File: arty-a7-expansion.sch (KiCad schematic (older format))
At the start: 61 parts, among them IC1 TPD8S009DSMR, J2 1140084168, J4 685119134923, J5 UE27AC54100, U1 TPS61232DRCT, U2 MAX3421EEHJ, Y1 KX-7_12.MHz

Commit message: Introduced schematic sections
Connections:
- net +3V3: now also C19.2; no longer C19.1
- net GND: now also C19.1; no longer C19.2
- net XI: now reaches C16.1, U2.24 (XI), Y1.1
- net XO: now reaches C17.1, U2.25 (XO), Y1.3
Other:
- note added: "Arty PMOD Connectors"
- note added: "USB controller"
- note removed: "HDMI Pmod connector"
- note removed: "SD card Pmod connector"
- note removed: "USB Pmod connector"
- moved on the sheet: C1, C10, C11, C12, C13, C14, C15, C16, C17, C18, C19, D1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

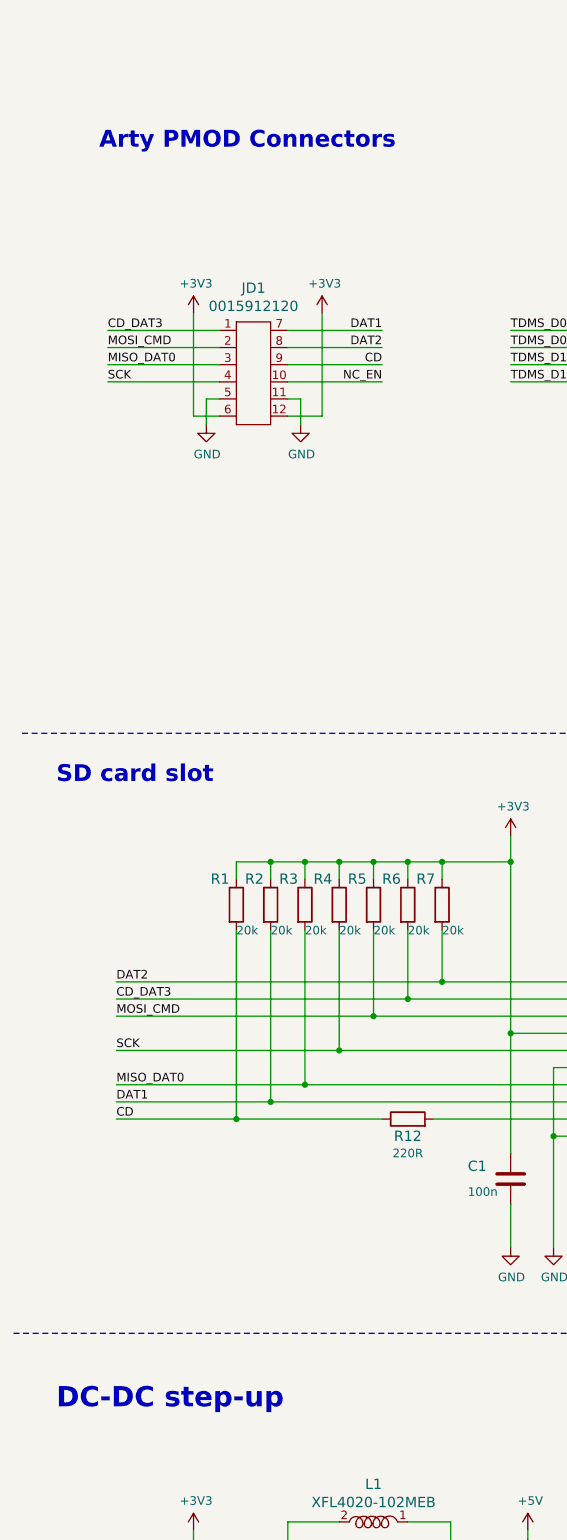
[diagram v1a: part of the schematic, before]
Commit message: Updated U1 MPN, updated layout around IC1
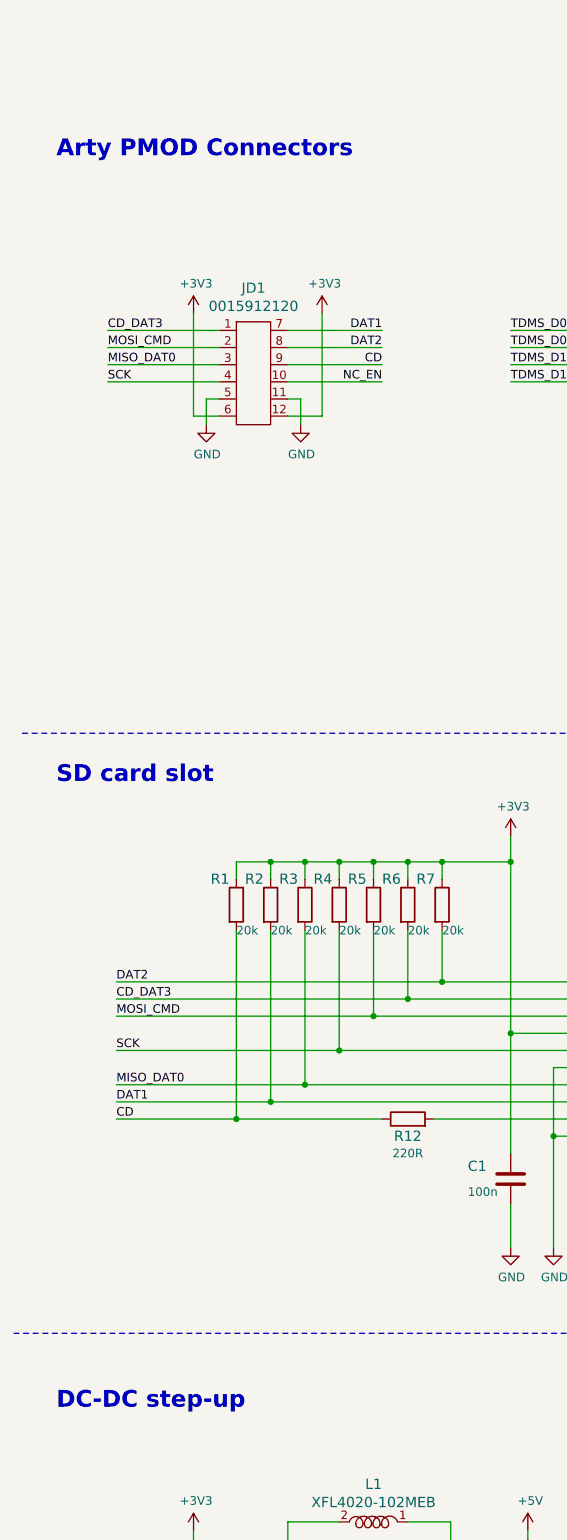
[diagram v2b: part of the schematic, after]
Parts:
- U1: MPN (none) -> TPS61232DRCT; Manufacturer (none) -> Texas Instruments

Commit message: Minor changes
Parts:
- added R23: R_0R_0603, arty-a7-expansion-footprints:0603-res, symbol arty-a7-expansion:R_0R_0603
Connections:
- net +3V3: now also R23.1
- net RST_USB: now also R23.2
- net D+: no longer names the net of R10.2, U2.21 (D+)
- net D-: no longer names the net of R9.2, U2.20 (D-)
- no-connect marks 0 -> 1
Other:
- note added: "DNP"
- moved on the sheet: J5, R10, R11, R9
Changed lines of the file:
@@
 $EndComp
-Wire Wire Line
-	12100 6950 11250 6950
 Wire Wire Line
 	12100 7050 11250 7050
@@
 Wire Wire Line
 	12100 7450 11250 7450
-Text Label 11250 6950 0    50   ~ 0
-RST_USB
 Text Label 11250 7050 0    50   ~ 0
 SCK_USB
@@
 	12700 5750 12700 5600
 Wire Wire Line
-	12100 6150 11850 6150
+	12100 6150 11950 6150
 $Comp
 L arty-a7-expansion:R_22R_0402 R9
 U 1 1 5D7A374A
-P 11350 6350
-F 0 "R9" H 11050 6400 60  0000 C CNN
-F 1 "R_22R_0402" H 11350 6200 60  0001 C CNN
-F 2 "arty-a7-expansion-footprints:0402-res" H 11550 6550 60  0001 L CNN
-F 3 "" H 11350 6350 50  0001 C CNN
-F 4 "VISHAY" H 11550 6750 60  0001 L CNN "Manufacturer"
-F 5 "CRCW040222R0FKED" H 11550 6650 60  0001 L CNN "MPN"
-F 6 "22R" H 11325 6350 50  0000 C CNN "Val"
-	1    11350 6350
+P 10650 6350
+F 0 "R9" H 10350 6400 60  0000 C CNN
+F 1 "R_22R_0402" H 10650 6200 60  0001 C CNN
+F 2 "arty-a7-expansion-footprints:0402-res" H 10850 6550 60  0001 L CNN
+F 3 "" H 10650 6350 50  0001 C CNN
+F 4 "VISHAY" H 10850 6750 60  0001 L CNN "Manufacturer"
+F 5 "CRCW040222R0FKED" H 10850 6650 60  0001 L CNN "MPN"
+F 6 "22R" H 10625 6350 50  0000 C CNN "Val"
+	1    10650 6350
 	1    0    0    -1
 $EndComp
@@
 L arty-a7-expansion:R_22R_0402 R10
 U 1 1 5D7A394F
-P 11350 6450
-F 0 "R10" H 11075 6375 60  0000 C CNN
-F 1 "R_22R_0402" H 11350 6300 60  0001 C CNN
-F 2 "arty-a7-expansion-footprints:0402-res" H 11550 6650 60  0001 L CNN
-F 3 "" H 11350 6450 50  0001 C CNN
-F 4 "VISHAY" H 11550 6850 60  0001 L CNN "Manufacturer"
-F 5 "CRCW040222R0FKED" H 11550 6750 60  0001 L CNN "MPN"
-F 6 "22R" H 11350 6450 50  0000 C CNN "Val"
-	1    11350 6450
+P 10650 6450
+F 0 "R10" H 10375 6375 60  0000 C CNN
+F 1 "R_22R_0402" H 10650 6300 60  0001 C CNN
+F 2 "arty-a7-expansion-footprints:0402-res" H 10850 6650 60  0001 L CNN
+F 3 "" H 10650 6450 50  0001 C CNN
+F 4 "VISHAY" H 10850 6850 60  0001 L CNN "Manufacturer"
+F 5 "CRCW040222R0FKED" H 10850 6750 60  0001 L CNN "MPN"
+F 6 "22R" H 10650 6450 50  0000 C CNN "Val"
+	1    10650 6450
 	1    0    0    -1
 $EndComp
@@
 L arty-a7-expansion:UE27AC54100 J5
 U 1 1 5D7BA5ED
-P 9050 6350
-F 0 "J5" V 8800 6650 60  0000 C CNN
-F 1 "UE27AC54100" V 8900 6400 60  0000 C CNN
-F 2 "arty-a7-expansion-footprints:USB_A_Female_UE27AC54100" H 9250 6550 60  0001 L CNN
-F 3 "https://www.amphenolcanada.com/ProductSearch/drawings/AC/UE27ACX4X0X.pdf" H 9250 6650 60  0001 L CNN
-F 4 "UE27AC54100" H 9250 6850 60  0001 L CNN "MPN"
-F 5 "Amphenol ICC (Commercial Products)" H 9250 7450 60  0001 L CNN "Manufacturer"
-	1    9050 6350
+P 8900 6350
+F 0 "J5" V 8650 6650 60  0000 C CNN
+F 1 "UE27AC54100" V 8750 6400 60  0000 C CNN
+F 2 "arty-a7-expansion-footprints:USB_A_Female_UE27AC54100" H 9100 6550 60  0001 L CNN
+F 3 "https://www.amphenolcanada.com/ProductSearch/drawings/AC/UE27ACX4X0X.pdf" H 9100 6650 60  0001 L CNN
+F 4 "UE27AC54100" H 9100 6850 60  0001 L CNN "MPN"
+F 5 "Amphenol ICC (Commercial Products)" H 9100 7450 60  0001 L CNN "Manufacturer"
+	1    8900 6350
 	1    0    0    1
 $EndComp
 Wire Wire Line
-	9500 6550 9350 6550
+	9500 6550 9200 6550
 $Comp
 L arty-a7-expansion:GND #PWR0109
@@
 $EndComp
 Wire Wire Line
-	9350 6450 9700 6450
+	9200 6450 9700 6450
 Wire Wire Line
 	9700 6450 9700 6600
@@
 	1500 10500 1500 10400
 Wire Wire Line
-	11850 6150 11850 6100
-Wire Wire Line
 	2200 10150 2100 10150
 Wire Wire Line
@@
 $EndComp
 Wire Wire Line
-	9350 6250 9350 5850
+	9200 6250 9200 5850
 $Comp
 L arty-a7-expansion:+5V #PWR0117
@@
 L arty-a7-expansion:R_10k_0603 R11
 U 1 1 5D77F979
-P 11850 5950
-F 0 "R11" V 11805 6020 60  0000 L CNN
-F 1 "R_10k_0603" H 11850 5800 60  0001 C CNN
-F 2 "arty-a7-expansion-footprints:0603-res" H 12050 6150 60  0001 L CNN
-F 3 "" H 11850 5950 50  0001 C CNN
-F 4 "BOURNS" H 12050 6350 60  0001 L CNN "Manufacturer"
-F 5 "CR0603-JW-103ELF" H 12050 6250 60  0001 L CNN "MPN"
-F 6 "10k" V 11903 6020 50  0000 L CNN "Val"
-	1    11850 5950
+P 11950 5500
+F 0 "R11" V 11800 5500 60  0000 L CNN
+F 1 "R_10k_0603" H 11950 5350 60  0001 C CNN
+F 2 "arty-a7-expansion-footprints:0603-res" H 12150 5700 60  0001 L CNN
+F 3 "" H 11950 5500 50  0001 C CNN
+F 4 "BOURNS" H 12150 5900 60  0001 L CNN "Manufacturer"
+F 5 "CR0603-JW-103ELF" H 12150 5800 60  0001 L CNN "MPN"
+F 6 "10k" V 12003 5570 50  0000 L CNN "Val"
+	1    11950 5500
 	0    1    1    0
 $EndComp
 Text Label 6950 2350 0    50   ~ 0
 GPX_USB
-Wire Wire Line
-	11850 6150 11250 6150
-Connection ~ 11850 6150
+Connection ~ 11950 6150
 Text Label 11250 6150 0    50   ~ 0
 INT_USB
 Text Label 7300 2550 2    50   ~ 0
 INT_USB
-$Comp
-L arty-a7-expansion:TP_SMD1MM TP5
-U 1 1 5D79AD74
-P 11150 6950
-F 0 "TP5" V 11150 6850 50  0000 C CNN
-F 1 "TP_SMD1MM" H 11150 6850 50  0001 C CNN
-F 2 "arty-a7-expansion-footprints:Testpoint_smd_1mm" H 11350 7150 60  0001 L CNN
-F 3 "" H 11350 7250 60  0001 L CNN
-	1    11150 6950
-	0    1    1    0
-$EndComp
 $Comp
 L arty-a7-expansion:TP_SMD1MM TP6
@@
 	1    0    0    -1
 $EndComp
-Text Label 11625 6450 0    50   ~ 0
-D+
-Text Label 11625 6350 0    50   ~ 0
-D-
-Text Label 10350 6350 0    50   ~ 0
+Text Label 9250 6350 0    50   ~ 0
 Data-
-Text Label 10350 6450 0    50   ~ 0
+Text Label 9250 6450 0    50   ~ 0
 Data+
 $Comp
@@
 	2900 6950 3900 6950
 Wire Wire Line
-	9175 6025 9500 6025
+	9025 6025 9500 6025
 Wire Wire Line
 	9500 6025 9500 6550
@@
 	9500 6550 9500 7150
 Wire Wire Line
-	11500 6450 12100 6450
-Wire Wire Line
-	11500 6350 12100 6350
+	10800 6450 12100 6450
+Wire Wire Line
+	10800 6350 12100 6350
 $Comp
 L arty-a7-expansion:+3V3 #PWR0112
@@
 	7750 8950 16050 8950
 Wire Wire Line
-	9700 6450 11200 6450
-Wire Wire Line
-	9350 6350 10000 6350
+	9700 6450 10500 6450
+Wire Wire Line
+	9200 6350 10000 6350
 Wire Wire Line
 	10000 6600 10000 6350
 Connection ~ 10000 6350
 Wire Wire Line
-	10000 6350 11200 6350
+	10000 6350 10500 6350
 $Comp
 L arty-a7-expansion:GND #PWR0131
@@
 	13750 5600 13750 5650
 $Comp
-L arty-a7-expansion:+3V3 #PWR0134
-U 1 1 5E79E54F
-P 11850 5600
-F 0 "#PWR0134" H 11850 5450 50  0001 C CNN
-F 1 "+3V3" H 11865 5773 50  0000 C CNN
-F 2 "" H 11850 5600 50  0001 C CNN
-F 3 "" H 11850 5600 50  0001 C CNN
-	1    11850 5600
-	1    0    0    -1
-$EndComp
-Wire Wire Line
-	11850 5600 11850 5800
-$Comp
 L arty-a7-expansion:GND #PWR0135
 U 1 1 5E7B2037
@@
 L arty-a7-expansion:+5V #PWR0138
 U 1 1 5E7FF960
-P 9350 5850
-F 0 "#PWR0138" H 9350 5700 50  0001 C CNN
-F 1 "+5V" H 9365 6023 50  0000 C CNN
-F 2 "" H 9350 5850 50  0001 C CNN
-F 3 "" H 9350 5850 50  0001 C CNN
-	1    9350 5850
+P 9200 5850
+F 0 "#PWR0138" H 9200 5700 50  0001 C CNN
+F 1 "+5V" H 9215 6023 50  0000 C CNN
+F 2 "" H 9200 5850 50  0001 C CNN
+F 3 "" H 9200 5850 50  0001 C CNN
+	1    9200 5850
 	1    0    0    -1
 $EndComp
@@
 	1    0    0    -1
 $EndComp
+NoConn ~ 9950 3000
+Text Label 11250 6950 0    50   ~ 0
+RST_USB
+$Comp
+L arty-a7-expansion:TP_SMD1MM TP5
+U 1 1 5D79AD74
+P 11150 6950
+F 0 "TP5" V 11150 6850 50  0000 C CNN
+F 1 "TP_SMD1MM" H 11150 6850 50  0001 C CNN
+F 2 "arty-a7-expansion-footprints:Testpoint_smd_1mm" H 11350 7150 60  0001 L CNN
+F 3 "" H 11350 7250 60  0001 L CNN
+	1    11150 6950
+	0    1    1    0
+$EndComp
+$Comp
+L arty-a7-expansion:R_0R_0603 R23
+U 1 1 5E716317
+P 11700 5500
+F 0 "R23" V 11550 5500 60  0000 L CNN
+F 1 "R_0R_0603" H 11700 5350 60  0001 C CNN
+F 2 "arty-a7-expansion-footprints:0603-res" H 11900 5700 60  0001 L CNN
+F 3 "" H 11700 5500 50  0001 C CNN
+F 4 "BOURNS" H 11900 5900 60  0001 L CNN "Manufacturer"
+F 5 "CR0603-J/-000ELF" H 11900 5800 60  0001 L CNN "MPN"
+F 6 "0R" V 11750 5550 50  0000 L CNN "Val"
+F 7 "1" V 11700 5500 50  0001 C CNN "DNP"
+	1    11700 5500
+	0    1    1    0
+$EndComp
+Wire Wire Line
+	11950 5250 11950 5350
+Connection ~ 11950 5250
+Wire Wire Line
+	11700 5250 11950 5250
+Wire Wire Line
+	11950 5150 11950 5250
+$Comp
+L arty-a7-expansion:+3V3 #PWR0134
+U 1 1 5E79E54F
+P 11950 5150
+F 0 "#PWR0134" H 11950 5000 50  0001 C CNN
+F 1 "+3V3" H 11965 5323 50  0000 C CNN
+F 2 "" H 11950 5150 50  0001 C CNN
+F 3 "" H 11950 5150 50  0001 C CNN
+	1    11950 5150
+	1    0    0    -1
+$EndComp
+Wire Wire Line
+	11250 6150 11950 6150
+Wire Wire Line
+	11700 5650 11700 6950
+Wire Wire Line
+	11950 5650 11950 6150
+Text Notes 11500 5400 0    50   ~ 0
+DNP
+Wire Wire Line
+	11700 5250 11700 5350
+Wire Wire Line
+	11250 6950 11700 6950
+Connection ~ 11700 6950
+Wire Wire Line
+	11700 6950 12100 6950
 $EndSCHEMATC

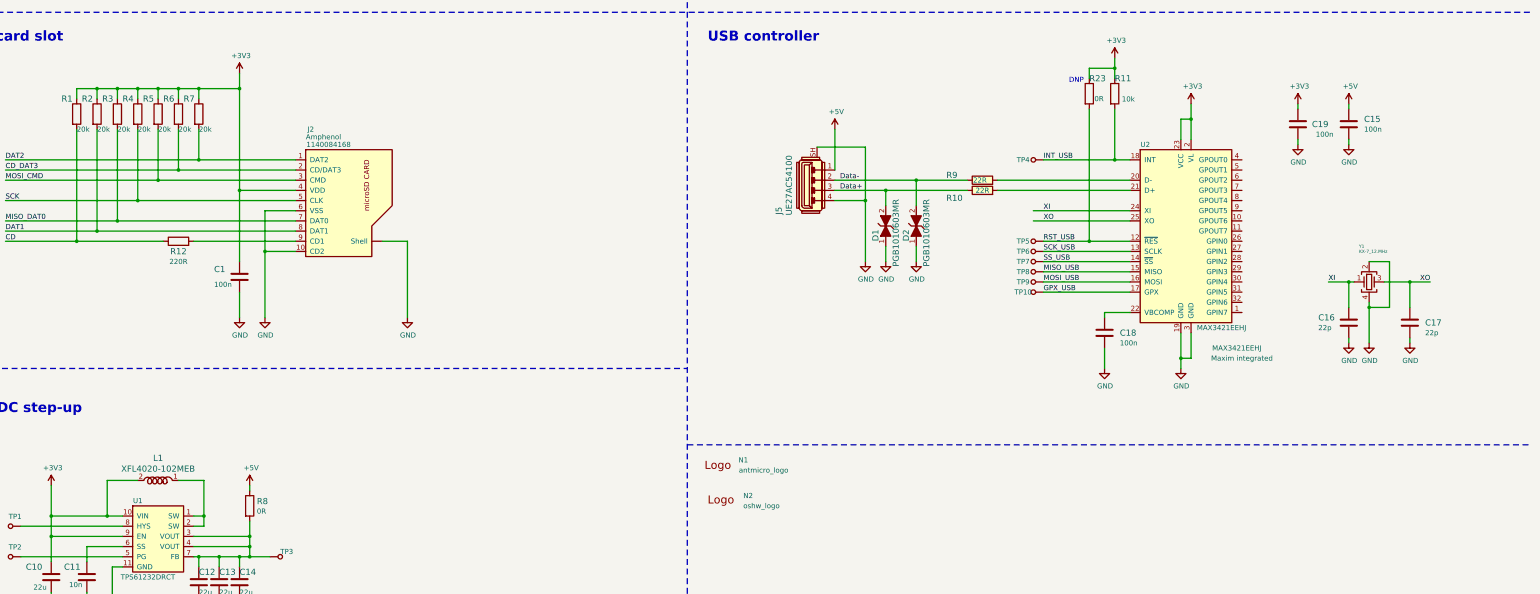
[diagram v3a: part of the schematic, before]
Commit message: Standardize components
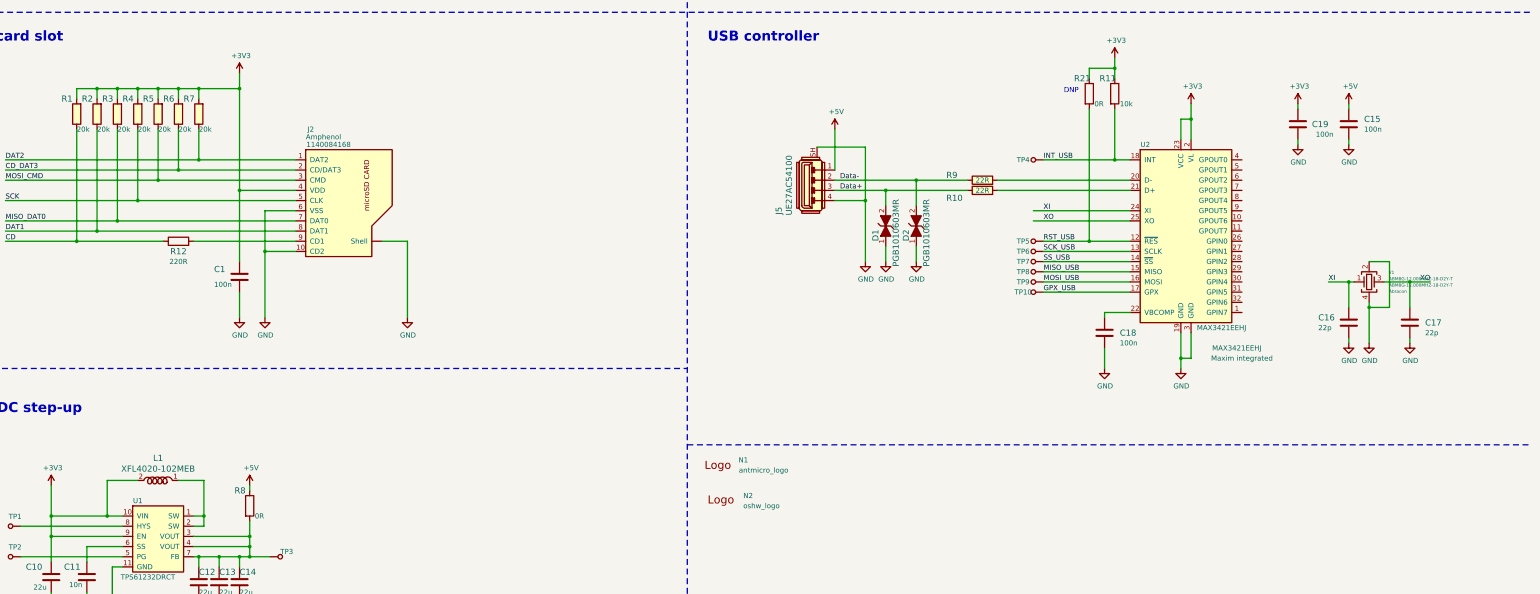
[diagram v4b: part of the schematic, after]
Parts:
- removed R1, R2, R3, R4, R5, R6, R7: R_20k_0603, arty-a7-expansion-footprints:0603-res, symbol arty-a7-expansion:R_20k_0603
- removed R11: R_10k_0603, arty-a7-expansion-footprints:0603-res, symbol arty-a7-expansion:R_10k_0603
- removed R23, R8: R_0R_0603, arty-a7-expansion-footprints:0603-res, symbol arty-a7-expansion:R_0R_0603
- removed Y1: KX-7_12.MHz, arty-a7-expansion-footprints:KX-7, symbol arty-a7-expansion:KX-7_12.MHz
- added R1, R2, R3, R4, R5, R6, R7: R_20k_0402, arty-a7-expansion-footprints:0402-res, symbol arty-a7-expansion:R_20k_0402
- added R11: R_10k_0402, arty-a7-expansion-footprints:0402-res, symbol arty-a7-expansion:R_10k_0402
- added R21, R8: R_0R_0402, arty-a7-expansion-footprints:0402-res, symbol arty-a7-expansion:R_0R_0402
- added Y1: ABM8G-12.000MHZ-18-D2Y-T, arty-a7-expansion-footprints:KX-7, symbol arty-a7-expansion:ABM8G-12.000MHZ-18-D2Y-T
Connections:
- net +3V3: now also R1.2, R11.1, R2.2, R21.1, R3.2, R4.2, R5.2, R6.2, R7.2
- net +5V: now also R8.1
- net CD: now also R1.1
- net CD_DAT3: now also R6.1
- net DAT1: now also R2.1
- net DAT2: now also R7.1
- net GND: now also Y1.2, Y1.4
- net INT_USB: now also R11.2
- net MISO_DAT0: now also R3.1
- net MOSI_CMD: now also R5.1
- net RST_USB: now also R21.2
- net SCK: now also R4.1
- net XI: now also Y1.1
- net XO: now also Y1.3
- net at C12.1, C13.1, C14.1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: now also R8.2

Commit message: Update mpn
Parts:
- C16, C17: MPN 160R15X106KV4E -> CC0402JRNPO9BN220; Manufacturer MULTICOMP -> YAGEO
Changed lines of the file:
@@
-$EndComp
-$Comp
-L arty-a7-expansion:C_22p_0402 C17
-U 1 1 5D8092BC
-P 14850 7750
-F 0 "C17" H 15000 7750 60  0000 L CNN
-F 1 "C_22p_0402" H 14850 7600 60  0001 C CNN
-F 2 "arty-a7-expansion-footprints:0402-cap" H 15050 7950 60  0001 L CNN
-F 3 "" H 14850 7750 50  0001 C CNN
-F 4 "MULTICOMP" H 15050 8150 60  0001 L CNN "Manufacturer"
-F 5 "160R15X106KV4E" H 15050 8050 60  0001 L CNN "MPN"
-F 6 "22p" H 15000 7650 50  0000 L CNN "Val"
-	1    14850 7750
-	1    0    0    -1
-$EndComp
-$Comp
-L arty-a7-expansion:C_22p_0402 C16
-U 1 1 5D80912A
-P 14250 7750
-F 0 "C16" H 13950 7800 60  0000 L CNN
-F 1 "C_22p_0402" H 14250 7600 60  0001 C CNN
-F 2 "arty-a7-expansion-footprints:0402-cap" H 14450 7950 60  0001 L CNN
-F 3 "" H 14250 7750 50  0001 C CNN
-F 4 "MULTICOMP" H 14450 8150 60  0001 L CNN "Manufacturer"
-F 5 "160R15X106KV4E" H 14450 8050 60  0001 L CNN "MPN"
-F 6 "22p" H 13950 7700 50  0000 L CNN "Val"
-	1    14250 7750
-	1    0    0    -1
 $EndComp
 $Comp
@@
 XI
 Wire Wire Line
-	14450 7550 14450 7600
-Wire Wire Line
 	14600 7350 14850 7350
-Text Label 14950 7350 0    50   ~ 0
+Text Label 15150 7350 0    50   ~ 0
 XO
-Wire Wire Line
-	14450 7150 14650 7150
-Wire Wire Line
-	14650 7150 14650 7600
-Wire Wire Line
-	14650 7600 14450 7600
-Connection ~ 14450 7600
 Wire Wire Line
 	14450 7600 14450 7950
 Connection ~ 14850 7350
 Wire Wire Line
-	14850 7350 15050 7350
+	14850 7350 15250 7350
 Wire Wire Line
 	14850 7600 14850 7350
@@
 	11700 6950 12100 6950
 $Comp
-L arty-a7-expansion:ABM8G-12.000MHZ-18-D2Y-T Y1
-U 1 1 5FA72836
-P 14450 7350
-F 0 "Y1" H 14644 7443 31  0000 L CNN
-F 1 "ABM8G-12.000MHZ-18-D2Y-T" H 14644 7381 31  0000 L CNN
-F 2 "arty-a7-expansion-footprints:KX-7" H 16550 7350 50  0001 C CNN
-F 3 "http://www.farnell.com/datasheets/1883677.pdf?_ga=2.231093087.191869416.1581926270-10679329.1579871714&_gac=1.250710644.1581676042.CjwKCAiAvonyBRB7EiwAadauqV_1bW_YqrahGYlcfSi9JhY_0bUtVM0CrC_Nr6PCzuK-nTMbciPOBxoCspAQAvD_BwE" H 16650 7450 50  0001 C CNN
-F 4 "ABM8G-12.000MHZ-18-D2Y-T " H 14644 7319 31  0000 L CNN "MPN"
-F 5 "Abracon" H 14644 7257 31  0000 L CNN "Manufacturer"
-	1    14450 7350
-	1    0    0    -1
-$EndComp
-$Comp
 L arty-a7-expansion:R_20k_0402 R1
 U 1 1 5FB1A4A7
@@
 	0    1    1    0
 $EndComp
+$Comp
+L arty-a7-expansion:C_22p_0402 C16
+U 1 1 5FC739F8
+P 14250 7750
+F 0 "C16" H 14050 7850 60  0000 L CNN
+F 1 "C_22p_0402" H 14250 7600 60  0001 C CNN
+F 2 "arty-a7-expansion-footprints:0402-cap" H 14450 7950 60  0001 L CNN
+F 3 "" H 14250 7750 50  0001 C CNN
+F 4 "YAGEO" H 14450 8150 60  0001 L CNN "Manufacturer"
+F 5 "CC0402JRNPO9BN220" H 14450 8050 60  0001 L CNN "MPN"
+F 6 "22p" H 14250 7650 50  0000 L CNN "Val"
+	1    14250 7750
+	1    0    0    -1
+$EndComp
+$Comp
+L arty-a7-expansion:C_22p_0402 C17
+U 1 1 5FC87210
+P 14850 7750
+F 0 "C17" H 14650 7850 60  0000 L CNN
+F 1 "C_22p_0402" H 14850 7600 60  0001 C CNN
+F 2 "arty-a7-expansion-footprints:0402-cap" H 15050 7950 60  0001 L CNN
+F 3 "" H 14850 7750 50  0001 C CNN
+F 4 "YAGEO" H 15050 8150 60  0001 L CNN "Manufacturer"
+F 5 "CC0402JRNPO9BN220" H 15050 8050 60  0001 L CNN "MPN"
+F 6 "22p" H 14850 7650 50  0000 L CNN "Val"
+	1    14850 7750
+	1    0    0    -1
+$EndComp
+Wire Wire Line
+	14450 7550 14450 7600
+Connection ~ 14450 7600
+$Comp
+L arty-a7-expansion:ABM8G-12.000MHZ-18-D2Y-T Y1
+U 1 1 5FA72836
+P 14450 7350
+F 0 "Y1" H 14644 7443 31  0000 L CNN
+F 1 "ABM8G-12.000MHZ-18-D2Y-T" H 14644 7381 31  0001 L CNN
+F 2 "arty-a7-expansion-footprints:KX-7" H 16550 7350 50  0001 C CNN
+F 3 "http://www.farnell.com/datasheets/1883677.pdf?_ga=2.231093087.191869416.1581926270-10679329.1579871714&_gac=1.250710644.1581676042.CjwKCAiAvonyBRB7EiwAadauqV_1bW_YqrahGYlcfSi9JhY_0bUtVM0CrC_Nr6PCzuK-nTMbciPOBxoCspAQAvD_BwE" H 16650 7450 50  0001 C CNN
+F 4 "ABM8G-12.000MHZ-18-D2Y-T " H 14644 7319 31  0001 L CNN "MPN"
+F 5 "Abracon" H 14644 7257 31  0001 L CNN "Manufacturer"
+	1    14450 7350
+	1    0    0    -1
+$EndComp
+Wire Wire Line
+	14450 7150 14450 7100
+Wire Wire Line
+	14450 7600 14650 7600
+Wire Wire Line
+	14450 7100 14650 7100
+Wire Wire Line
+	14650 7100 14650 7600
 $EndSCHEMATC
